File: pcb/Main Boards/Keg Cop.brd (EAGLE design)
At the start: 51.3 x 51 mm, 28 parts

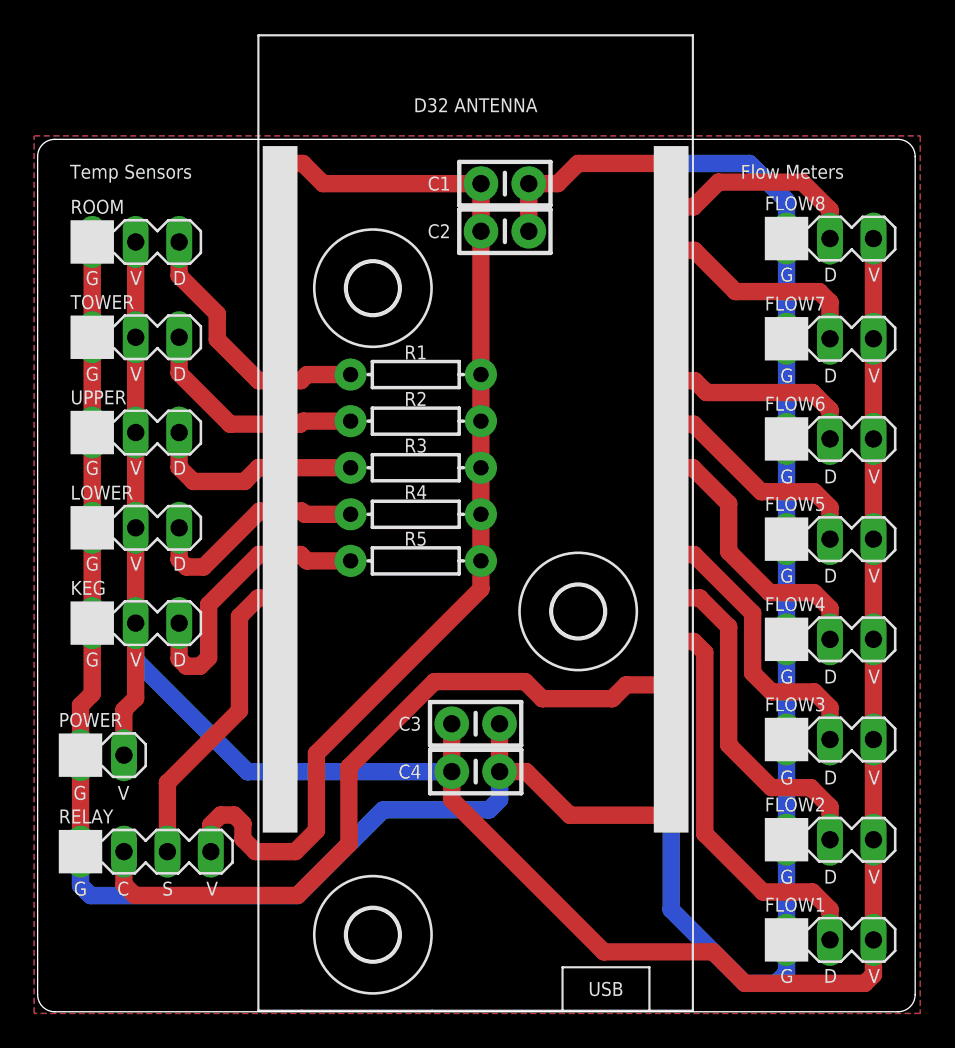
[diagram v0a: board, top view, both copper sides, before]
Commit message: Swap pins, split dirs
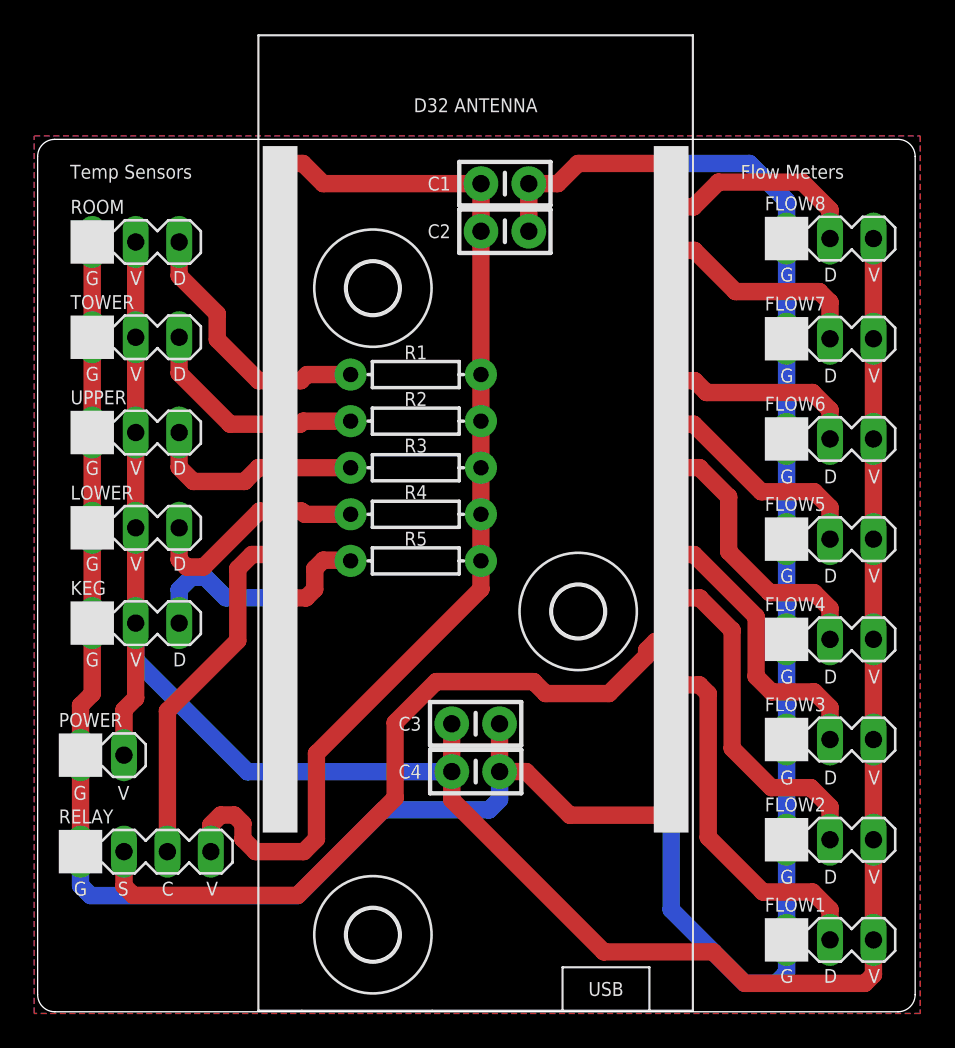
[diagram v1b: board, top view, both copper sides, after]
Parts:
- D32: value (none) -> U1
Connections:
- net COOL: now also D32.IO27, RELAY.3; no longer D32.IO0, RELAY.2
- net KDAT: now also D32.IO14; no longer D32.IO27
- net KEG1: now also D32.IO0; no longer D32.IO4
- net SOL: now also D32.IO4, RELAY.2; no longer D32.IO14, RELAY.3
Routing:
- net SOL: track 18.3 -> 43.7 mm
- net COOL: track 42.7 -> 21.1 mm
- net KDAT: track 17.0 -> 14.4 mm
- net KEG1: track 23.8 -> 21.4 mm
